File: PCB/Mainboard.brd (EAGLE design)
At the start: 92.9 x 26.7 mm, 23 parts, among them T1 RM2302, T2 RM2302, T3 RM2302

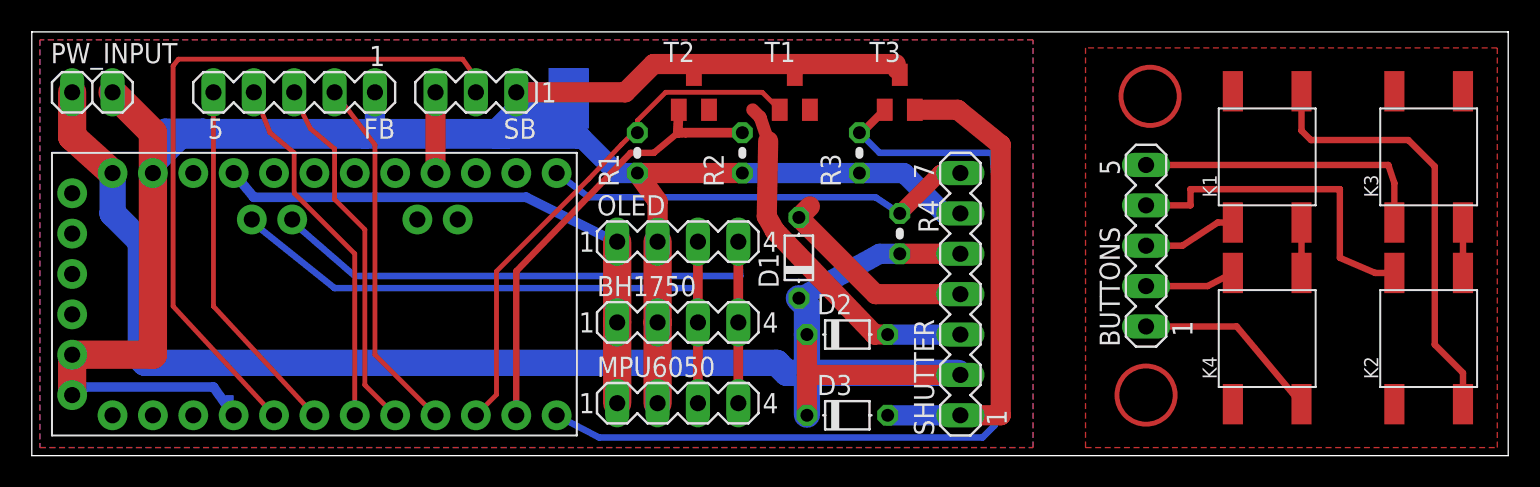
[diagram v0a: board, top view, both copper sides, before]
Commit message: Add vias to get around the transistor routing issue
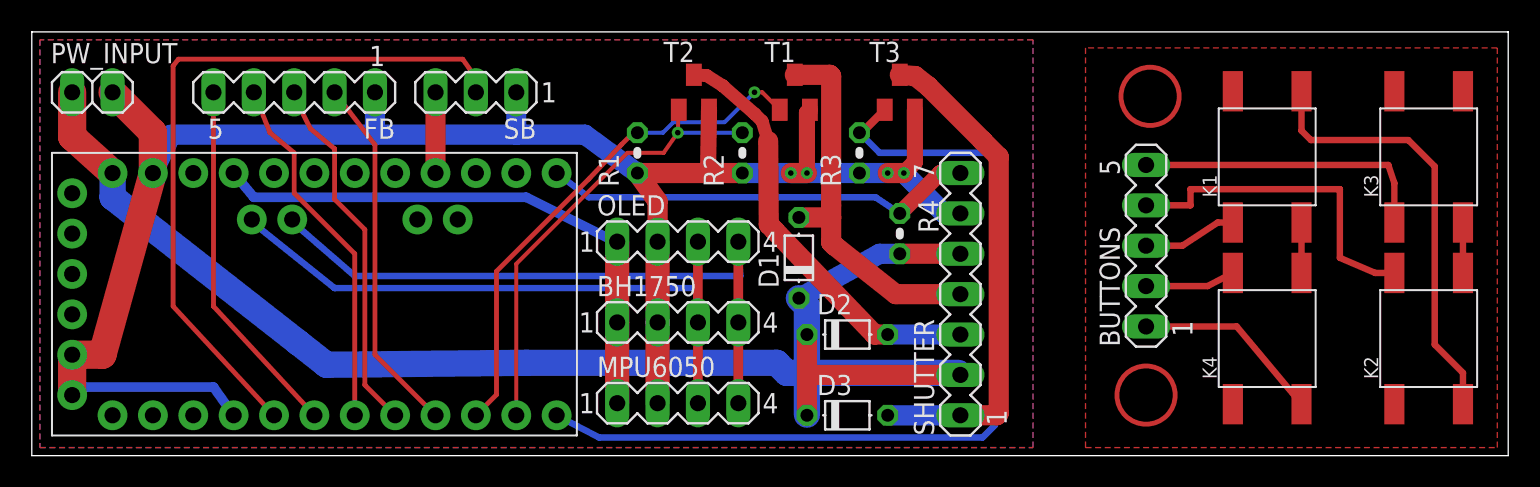
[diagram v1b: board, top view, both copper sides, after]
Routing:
- net GND: track 171.8 -> 121.5 mm, vias 0 -> 4
- net S2: track 13.1 -> 24.1 mm
- net VCC: track 103.8 -> 98.2 mm
- net S1: track 22.5 -> 26.9 mm
- net N$2: track 30.5 -> 28.7 mm, vias 0 -> 1
- net M_GND: track 29.7 -> 31.5 mm
- net N$3: track 33.0 -> 32.6 mm, vias 0 -> 1

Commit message: Add voltage sense line for battery
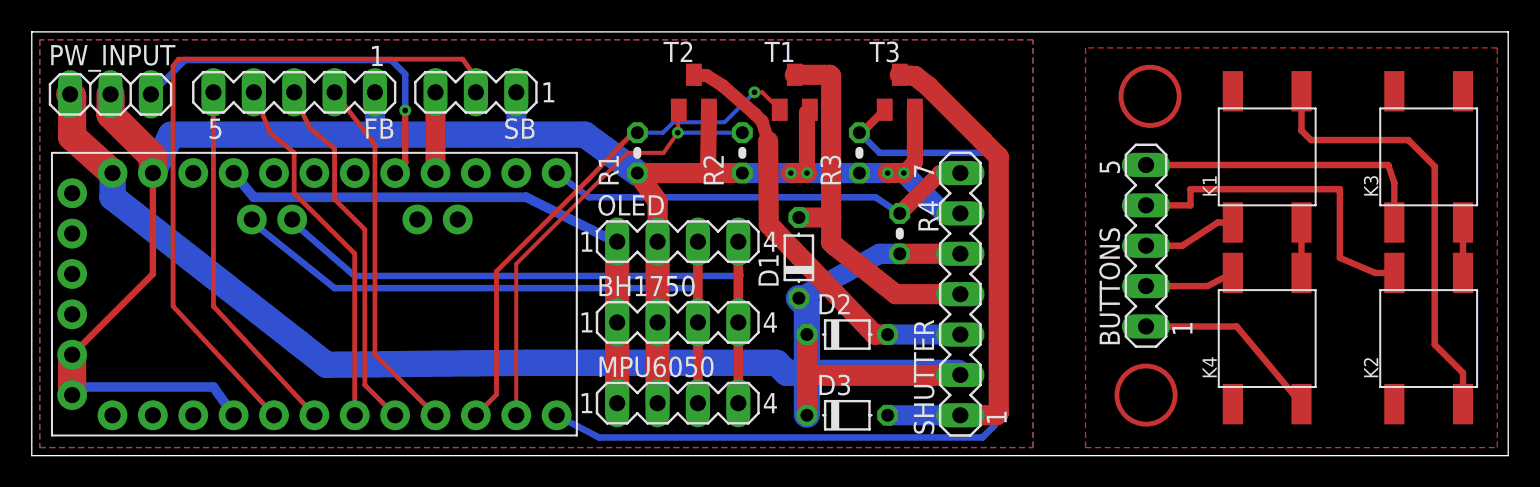
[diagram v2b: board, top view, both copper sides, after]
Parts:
- PW_INPUT: device pinhead:1X02 -> pinhead:1X03
- moved PW_INPUT 1.15 mm to (4.95, 22.7)
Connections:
- new net BAT_SENSE: PW_INPUT.3, U$7.A0
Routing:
- net BAT_SENSE: track 0.00 -> 23.8 mm, vias 0 -> 1
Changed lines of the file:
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@@
 <layer number="19" name="Unrouted" color="6" fill="1" visible="yes" active="yes"/>
 <layer number="20" name="Dimension" color="24" fill="1" visible="yes" active="yes"/>
-<layer number="21" name="tPlace" color="7" fill="1" visible="no" active="yes"/>
-<layer number="22" name="bPlace" color="7" fill="1" visible="no" active="yes"/>
-<layer number="23" name="tOrigins" color="15" fill="1" visible="no" active="yes"/>
-<layer number="24" name="bOrigins" color="15" fill="1" visible="no" active="yes"/>
-<layer number="25" name="tNames" color="7" fill="1" visible="no" active="yes"/>
-<layer number="26" name="bNames" color="7" fill="1" visible="no" active="yes"/>
-<layer number="27" name="tValues" color="7" fill="1" visible="no" active="yes"/>
-<layer number="28" name="bValues" color="7" fill="1" visible="no" active="yes"/>
+<layer number="21" name="tPlace" color="7" fill="1" visible="yes" active="yes"/>
+<layer number="22" name="bPlace" color="7" fill="1" visible="yes" active="yes"/>
+<layer number="23" name="tOrigins" color="15" fill="1" visible="yes" active="yes"/>
+<layer number="24" name="bOrigins" color="15" fill="1" visible="yes" active="yes"/>
+<layer number="25" name="tNames" color="7" fill="1" visible="yes" active="yes"/>
+<layer number="26" name="bNames" color="7" fill="1" visible="yes" active="yes"/>
+<layer number="27" name="tValues" color="7" fill="1" visible="yes" active="yes"/>
+<layer number="28" name="bValues" color="7" fill="1" visible="yes" active="yes"/>
 <layer number="29" name="tStop" color="7" fill="3" visible="yes" active="yes"/>
 <layer number="30" name="bStop" color="7" fill="6" visible="yes" active="yes"/>
@@
 <element name="MPU6050" library="infineon" package="MA04-1" value="MPU-6050" x="40.64" y="3.302"/>
 <element name="OLED" library="infineon" package="MA04-1" value="OLED" x="40.64" y="13.462"/>
-<element name="PW_INPUT" library="pinhead" library_urn="urn:adsk.eagle:library:325" package="1X02" package3d_urn="urn:adsk.eagle:package:22435/2" value="" x="3.81" y="22.86"/>
+<element name="PW_INPUT" library="pinhead" library_urn="urn:adsk.eagle:library:325" package="1X03" package3d_urn="urn:adsk.eagle:package:22458/2" value="" x="4.953" y="22.733"/>
 <element name="R1" library="rcl" library_urn="urn:adsk.eagle:library:334" package="0204V" package3d_urn="urn:adsk.eagle:package:23495/1" value="660" x="38.1" y="19.05" rot="R90"/>
 <element name="R2" library="rcl" library_urn="urn:adsk.eagle:library:334" package="0204V" package3d_urn="urn:adsk.eagle:package:23495/1" value="660" x="44.704" y="19.05" rot="R90"/>
@@
 <wire x1="3.048" y1="3.81" x2="3.302" y2="4.318" width="0.6096" layer="16"/>
 <wire x1="3.302" y1="4.318" x2="11.43" y2="4.318" width="0.6096" layer="16"/>
-<wire x1="7.62" y1="20.32" x2="5.08" y2="22.86" width="1.778" layer="1"/>
-<wire x1="7.62" y1="17.78" x2="7.62" y2="20.32" width="1.778" layer="1"/>
-<wire x1="4.445" y1="6.35" x2="2.54" y2="6.35" width="1.778" layer="1"/>
-<wire x1="7.62" y1="17.78" x2="4.445" y2="6.35" width="1.778" layer="1"/>
 <wire x1="39.37" y1="13.462" x2="39.37" y2="16.002" width="1.27" layer="1"/>
 <wire x1="38.1" y1="17.78" x2="39.37" y2="16.002" width="1.27" layer="1"/>
@@
 <wire x1="55.56" y1="18.476" x2="54.864" y2="17.78" width="1.016" layer="1"/>
 <wire x1="30.48" y1="22.86" x2="30.48" y2="20.193" width="1.27" layer="16"/>
-<wire x1="30.48" y1="20.193" x2="21.59" y2="20.193" width="1.27" layer="16"/>
-<wire x1="21.59" y1="20.193" x2="8.763" y2="20.193" width="1.27" layer="16"/>
-<wire x1="8.763" y1="20.193" x2="7.62" y2="17.78" width="1.27" layer="16"/>
+<wire x1="30.48" y1="20.193" x2="21.59" y2="20.193" width="1.651" layer="16"/>
+<wire x1="21.59" y1="20.193" x2="8.763" y2="20.193" width="1.651" layer="16"/>
+<wire x1="8.763" y1="20.193" x2="7.62" y2="17.78" width="1.651" layer="16"/>
 <wire x1="21.59" y1="20.193" x2="21.59" y2="22.86" width="1.27" layer="16"/>
-<wire x1="30.48" y1="20.193" x2="34.798" y2="20.193" width="1.27" layer="16"/>
-<wire x1="34.798" y1="20.193" x2="38.1" y2="17.78" width="1.27" layer="16"/>
+<wire x1="30.48" y1="20.193" x2="34.798" y2="20.193" width="1.651" layer="16"/>
+<wire x1="34.798" y1="20.193" x2="38.1" y2="17.78" width="1.651" layer="16"/>
+<wire x1="7.62" y1="17.78" x2="7.62" y2="18.796" width="1.778" layer="1"/>
+<wire x1="4.953" y1="21.463" x2="4.953" y2="22.733" width="1.778" layer="1"/>
+<wire x1="7.62" y1="18.796" x2="4.953" y2="21.463" width="1.778" layer="1"/>
+<wire x1="7.62" y1="17.78" x2="7.62" y2="11.43" width="0.4064" layer="1"/>
+<wire x1="7.62" y1="11.43" x2="2.54" y2="6.35" width="0.4064" layer="1"/>
 </signal>
 <signal name="N$1">
@@
 <contactref element="D1" pad="C"/>
 <contactref element="U$7" pad="RAW"/>
-<wire x1="2.54" y1="20.066" x2="2.54" y2="22.86" width="1.778" layer="1"/>
 <wire x1="5.08" y1="17.78" x2="2.54" y2="20.066" width="1.778" layer="1"/>
 <wire x1="48.26" y1="9.906" x2="53.34" y2="12.7" width="1.27" layer="16"/>
@@
 <wire x1="48.768" y1="7.62" x2="48.768" y2="9.398" width="1.651" layer="16"/>
 <wire x1="48.768" y1="9.398" x2="48.26" y2="9.906" width="1.651" layer="16"/>
+<wire x1="2.54" y1="20.066" x2="2.54" y2="22.606" width="1.778" layer="1"/>
+<wire x1="2.54" y1="22.606" x2="2.413" y2="22.733" width="1.778" layer="1"/>
 </signal>
 <signal name="S2">
@@
 <wire x1="36.83" y1="13.462" x2="36.703" y2="13.462" width="0.6096" layer="16"/>
 </signal>
+<signal name="BAT_SENSE">
+<contactref element="PW_INPUT" pad="3"/>
+<contactref element="U$7" pad="A0"/>
+<via x="23.495" y="21.717" extent="1-16" drill="0.35"/>
+<wire x1="22.86" y1="17.78" x2="23.495" y2="18.415" width="0.4064" layer="1"/>
+<wire x1="23.495" y1="18.415" x2="23.495" y2="21.717" width="0.4064" layer="1"/>
+<wire x1="7.493" y1="22.733" x2="9.652" y2="24.892" width="0.4064" layer="16"/>
+<wire x1="9.652" y1="24.892" x2="22.606" y2="24.892" width="0.4064" layer="16"/>
+<wire x1="22.606" y1="24.892" x2="23.495" y2="24.003" width="0.4064" layer="16"/>
+<wire x1="23.495" y1="24.003" x2="23.495" y2="21.717" width="0.4064" layer="16"/>
+</signal>
 </signals>
